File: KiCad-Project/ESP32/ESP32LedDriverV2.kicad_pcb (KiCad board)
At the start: 4 copper layers, 100 x 56.7 mm, 55 parts, among them J1 Power, J2 LED Terminal, J3 UART, Q1 Q_PMOS_GDS, Q10 Q_NMOS_GDS, Q2 S8050, Q3 Q_NMOS_GDS, Q4 Q_NMOS_GDS, Q5 Q_NMOS_GDS, Q6 Q_NMOS_GDS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

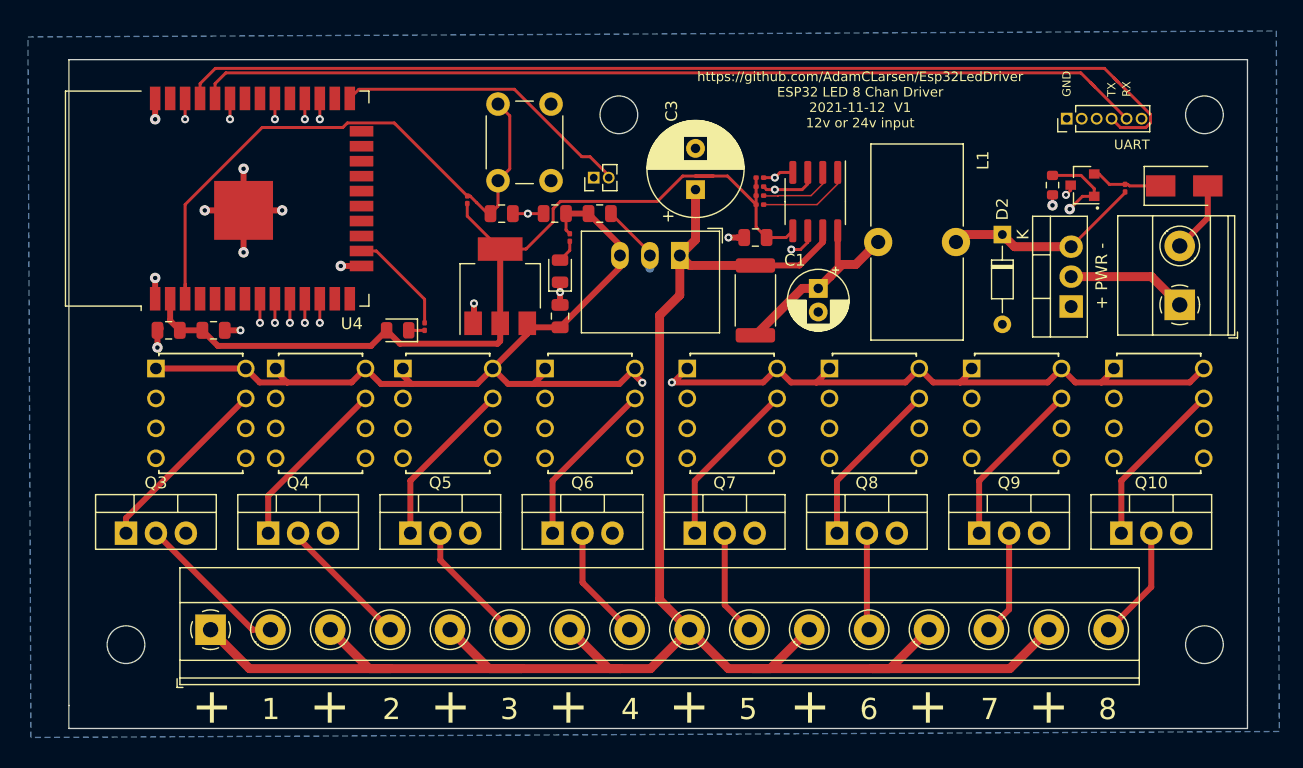
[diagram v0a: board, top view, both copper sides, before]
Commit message: swap out 603 resistors for 805
Give us more room to work with if we have to fix something.
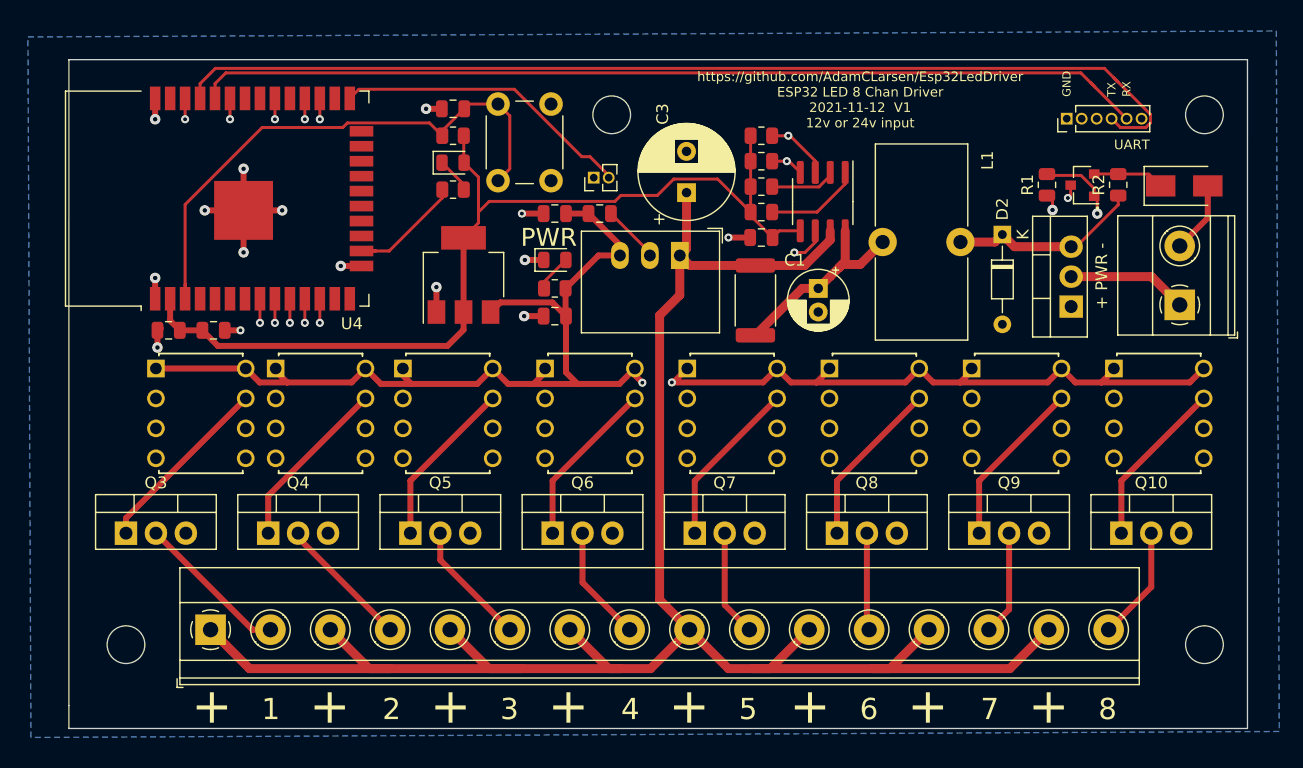
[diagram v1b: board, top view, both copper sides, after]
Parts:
- R1: footprint Resistor_SMD:R_0603_1608Metric -> Resistor_SMD:R_0805_2012Metric
- R10, R2, R4, R5, R6, R7, R8, R9: footprint Resistor_SMD:R_0201_0603Metric -> Resistor_SMD:R_0805_2012Metric
- moved LED2 15.0 mm to (77.0, 71.4), turned to 0 degrees
- moved R10 11.9 mm to (77.0, 73.7), turned to 0 degrees
- moved C6 9.81 mm to (77.0, 66.8), turned to 180 degrees
- moved R9 5.56 mm to (77.0, 69.1), turned to 180 degrees
- moved R8 4.50 mm to (85.6, 82.0), turned to 180 degrees
- moved R4 4.32 mm to (103.1, 69.1)
- moved U3 3.25 mm to (77.9, 80.9)
- moved R5 1.40 mm to (103.1, 71.2)
- moved LED1 1.05 mm to (85.6, 79.6), turned to 0 degrees
- moved C3 0.80 mm to (96.8, 73.9)
- moved R7 0.77 mm to (103.1, 73.4)
- moved R2 0.65 mm to (133.4, 73.3)
- moved R6 0.65 mm to (103.1, 75.6)
- moved U1 0.64 mm to (108.3, 74.7)
- moved H3 0.61 mm to (90.4, 67.3)
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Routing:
- net /ESP32/~RESET: track 51.4 -> 47.8 mm
- net +5V: track 132.5 -> 136.0 mm
- net SCL: track 59.5 -> 62.5 mm
- net +3V3: track 80.8 -> 83.7 mm
- net GND: track 50.1 -> 52.6 mm, vias 15 -> 17
- net Net-(LED2-Pad1): track 1.35 -> 3.05 mm
- net Net-(R10-Pad1): track 9.05 -> 10.7 mm
- net Net-(LED1-Pad2): track 1.94 -> 3.18 mm
- net Net-(Q1-Pad1): track 16.6 -> 15.6 mm
- net Net-(R7-Pad2): track 6.42 -> 5.61 mm
- net +24V_SW: track 17.8 -> 18.3 mm
- net +24V_IN: track 17.8 -> 18.3 mm
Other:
- board text added: "PWR"

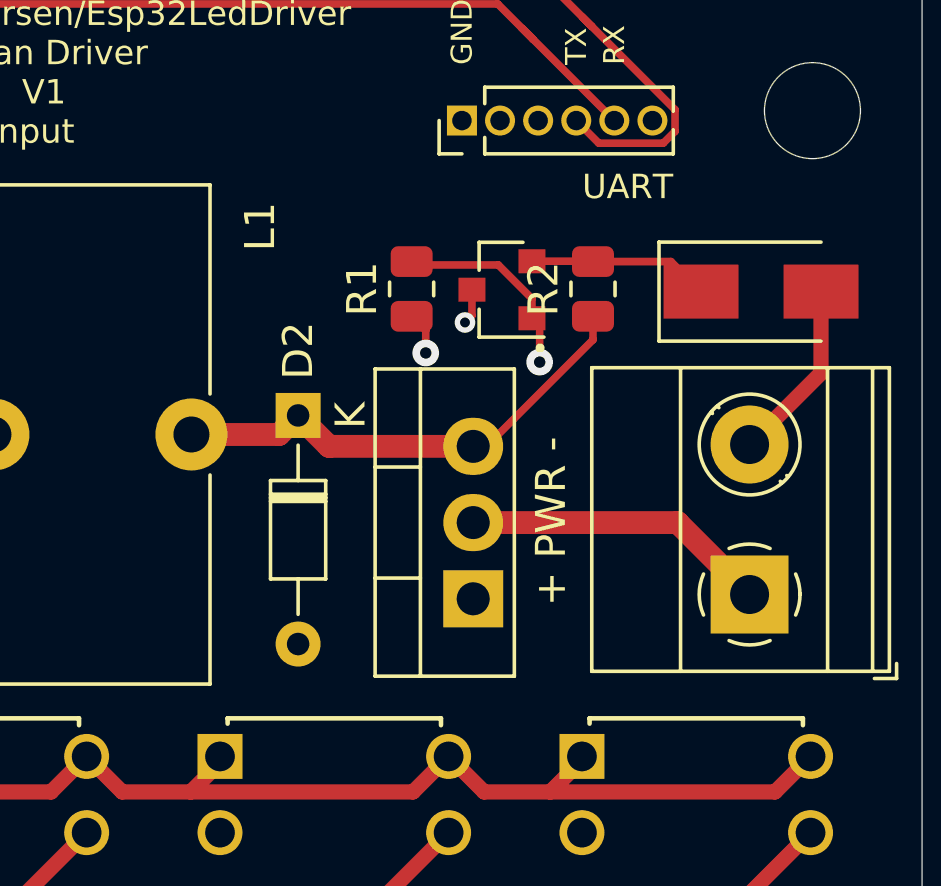
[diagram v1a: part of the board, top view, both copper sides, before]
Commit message: Switch power direction detection to SMD
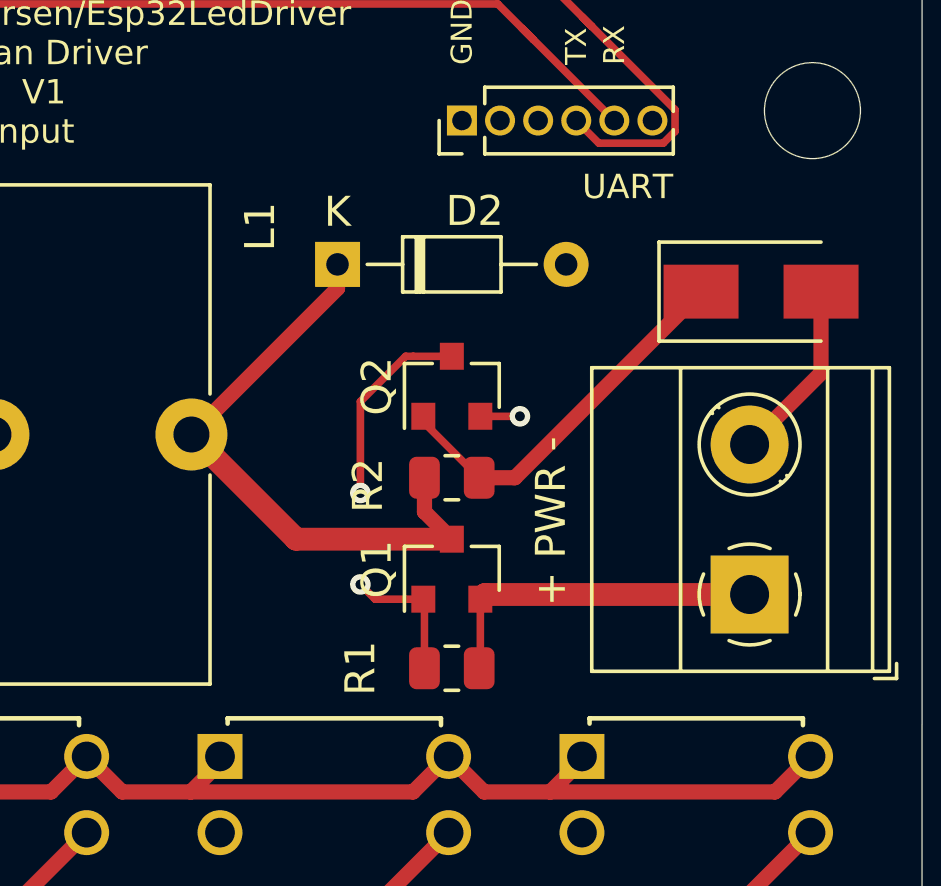
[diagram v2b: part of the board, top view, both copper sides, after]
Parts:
- Q1: value Q_PMOS_GDS -> PMOS 30V; footprint Package_TO_SOT_THT:TO-220-3_Vertical -> Package_TO_SOT_SMD:SOT-23
- moved R1 12.7 mm to (128.7, 85.9), turned to 180 degrees
- moved R2 7.86 mm to (128.7, 79.5), turned to 0 degrees
- moved D2 5.20 mm to (124.9, 72.4), turned to 0 degrees
- moved Q2 3.63 mm to (128.7, 76.5), turned to 90 degrees
- moved Q1 1.22 mm to (128.7, 82.6)
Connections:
- Q2 pad 1: Net-(Q1-Pad1) -> Net-(D1-Pad1)
- Q2 pad 2: Net-(D1-Pad1) -> GND
- Q2 pad 3: GND -> Net-(Q1-Pad1)
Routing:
- net Net-(D1-Pad1): track 6.06 -> 12.8 mm
- net /+24V_RAW: track 17.9 -> 11.4 mm, vias 1 -> 0
- net +24V_SW: track 18.3 -> 21.1 mm
- net Net-(Q1-Pad1): track 15.6 -> 14.4 mm, vias 1 -> 2

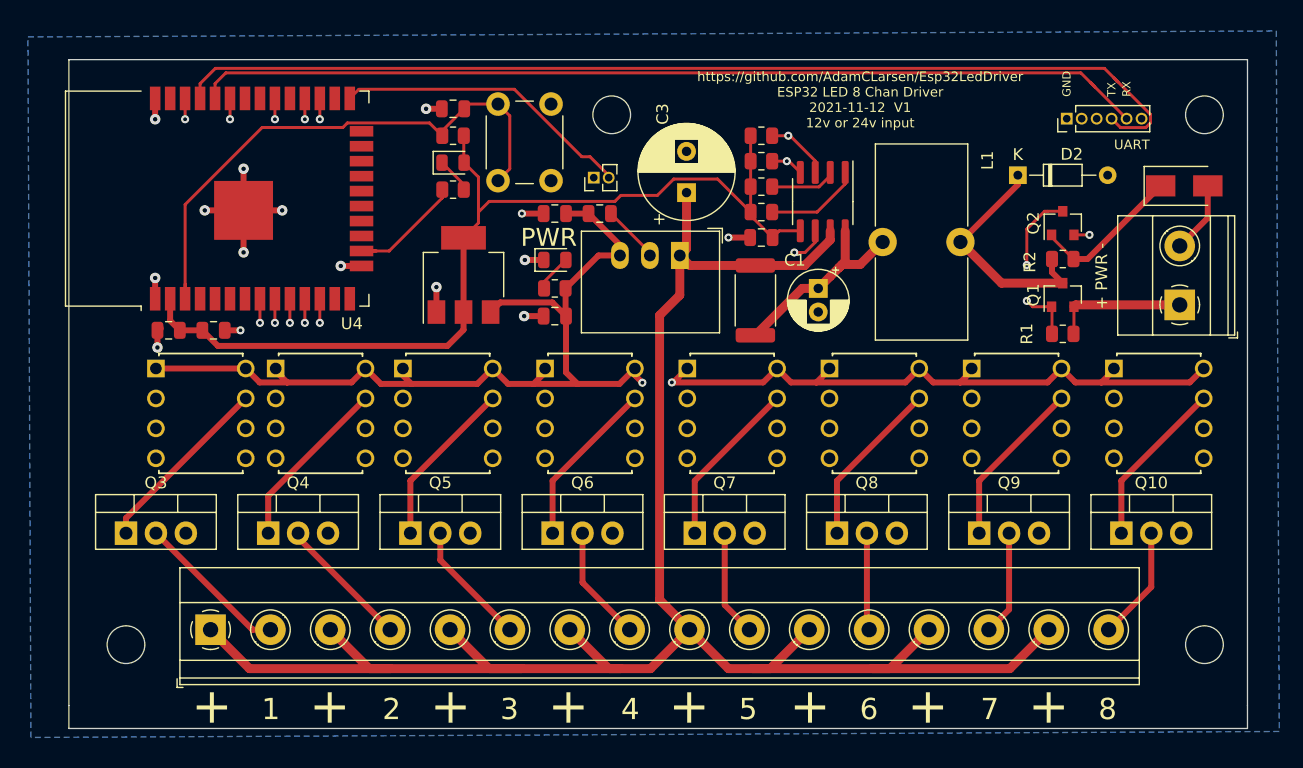
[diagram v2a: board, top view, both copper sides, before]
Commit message: Fixes in prep for printing
Making sure tolerance are in-spec for JLC PCB
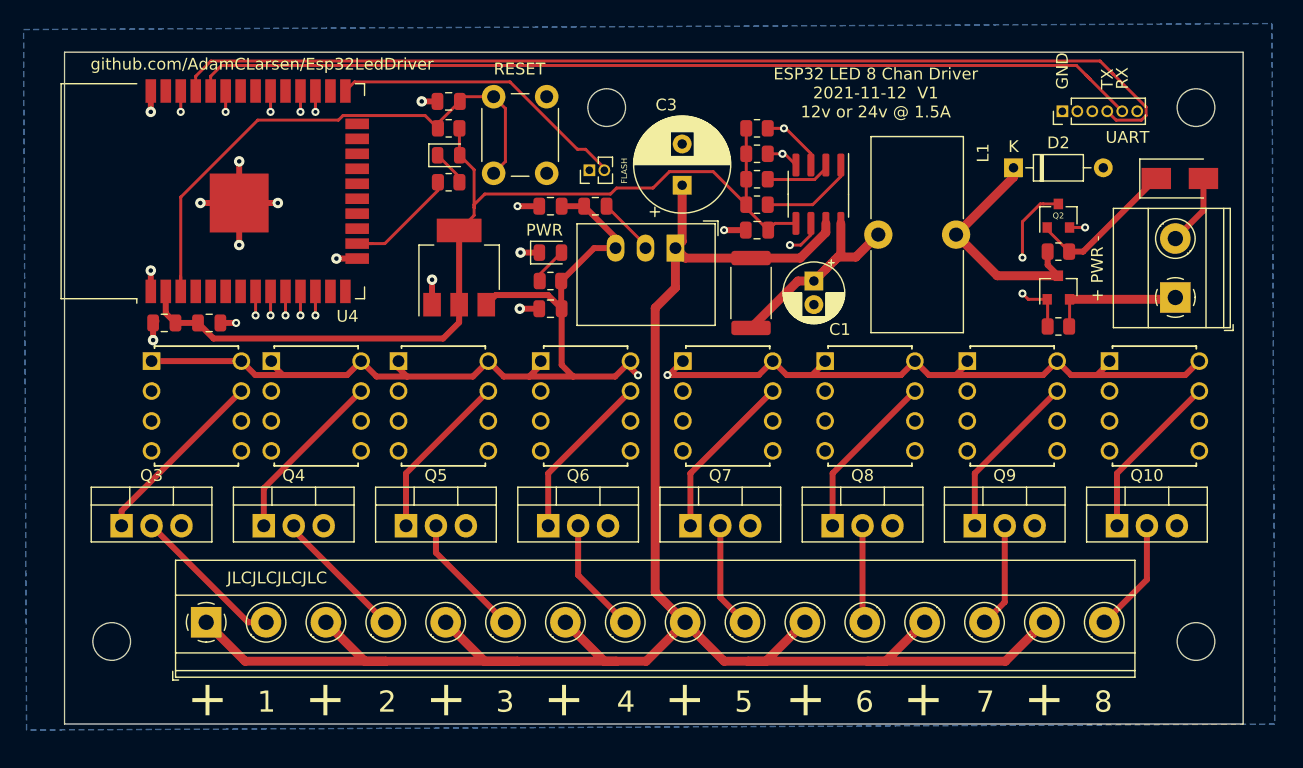
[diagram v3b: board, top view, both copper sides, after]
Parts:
- D2: footprint Diode_THT:D_DO-34_SOD68_P7.62mm_Horizontal -> Diode_THT:D_DO-35_SOD27_P7.62mm_Horizontal
- R3: value 100 ±1% 1W -> 0.1Ω 1% 1W
- moved H1 1.24 mm to (48.0, 112.0)
- moved H4 0.94 mm to (140.0, 66.7)
- moved H2 0.76 mm to (140.0, 112.0)
- moved H3 0.74 mm to (90.0, 66.7)
- moved U11 0.73 mm to (128.2, 95.8)
- moved U12 0.73 mm to (140.3, 95.8)
- moved C1 0.73 mm to (107.6, 81.4)
- moved C2 0.73 mm to (102.8, 77.1)
- moved C3 0.73 mm to (96.4, 73.3)
- moved C6 0.73 mm to (76.6, 66.2)
- moved C8 0.73 mm to (52.5, 85.0)
- moved C9 0.73 mm to (56.3, 85.0)
- moved D2 0.73 mm to (124.5, 71.8)
- moved J2 0.73 mm to (56.0, 110.4)
- moved JP1 0.73 mm to (88.5, 72.0)
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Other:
- board size 100 x 56.7 mm -> 100 x 57 mm
- board text added: "ESP32 LED 8 Chan Driver 2021-11-12 V1 12v or 24v @ 1.5A"
- board text added: "FLASH"
- board text added: "JLCJLCJLCJLC"
- board text added: "RESET"
- board text added: "github.com/AdamCLarsen/Esp32LedDriver"
- board text removed: "https://github.com/AdamCLarsen/Esp32LedDriver ESP32 LED 8 Chan Driver 2021-11-12 V1 12v or 24v input"

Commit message: Fix Power Mosfet direction
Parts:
- turned Q1 to 270 degrees
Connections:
- Q1 pad 2: /+24V_RAW -> +24V_SW
- Q1 pad 3: +24V_SW -> /+24V_RAW
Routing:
- net Net-(Q1-Pad1): track 14.4 -> 18.9 mm
- net /+24V_RAW: track 11.4 -> 12.7 mm
- net +24V_SW: track 21.1 -> 19.8 mm
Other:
- board text added: "ESP32 LED 8 Chan Driver 2021-11-14 V1 12v or 24v @ 1.5A"
- board text removed: "ESP32 LED 8 Chan Driver 2021-11-12 V1 12v or 24v @ 1.5A"

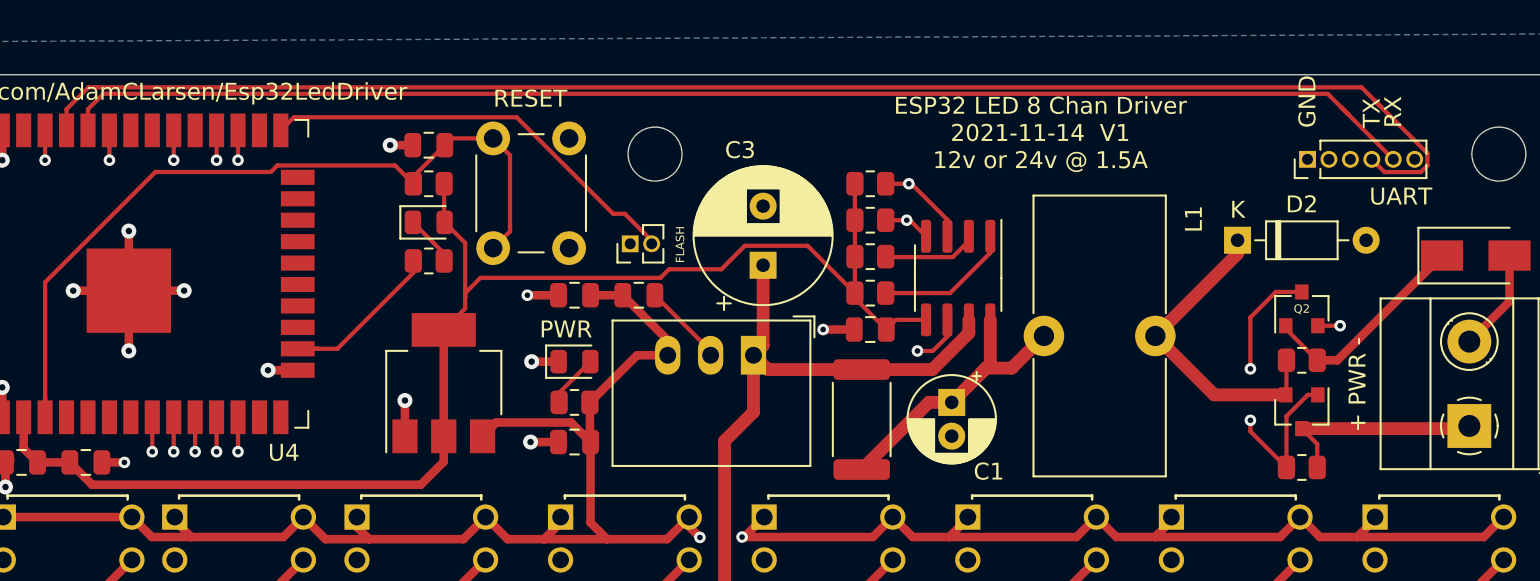
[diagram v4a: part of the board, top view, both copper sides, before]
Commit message: Fix pin header
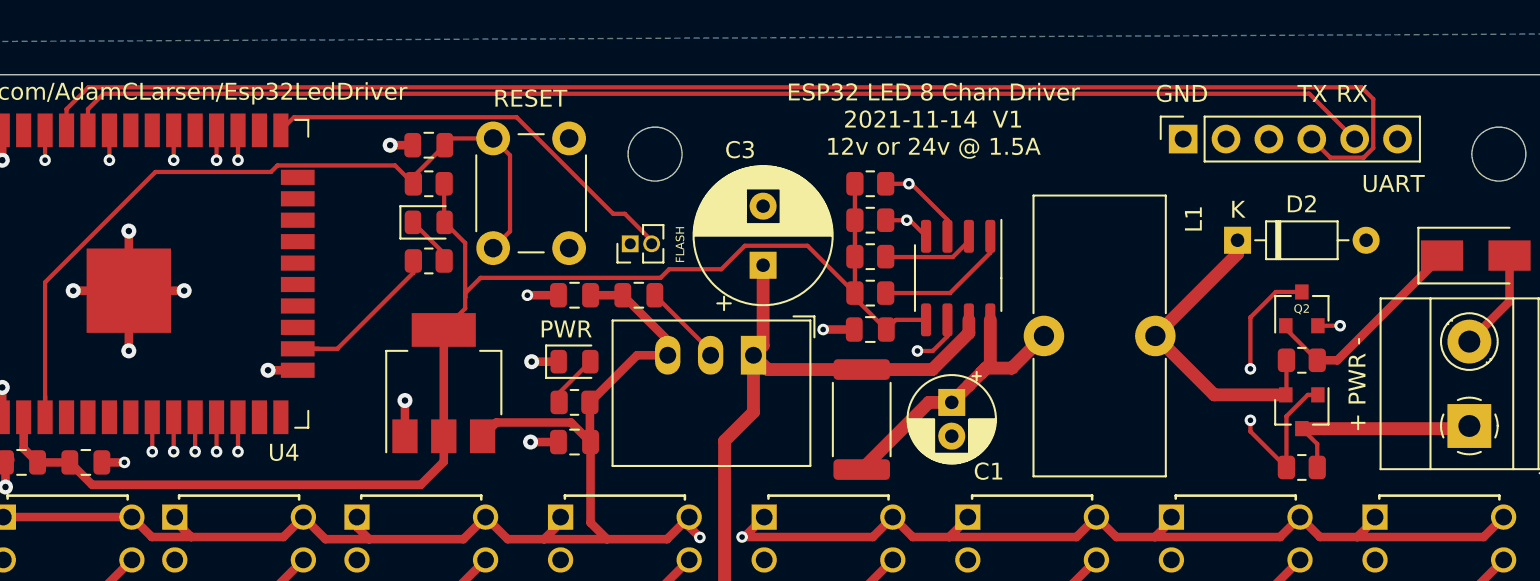
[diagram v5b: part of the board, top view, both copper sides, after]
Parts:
- J3: footprint Connector_PinHeader_1.27mm:PinHeader_1x06_P1.27mm_Vertical -> Connector_PinSocket_2.54mm:PinSocket_1x06_P2.54mm_Vertical
- moved J3 7.47 mm to (121.3, 65.8)
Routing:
- net /ESP32/UART_RX: track 81.1 -> 77.8 mm
- net /ESP32/UART_TX: track 89.0 -> 86.7 mm
